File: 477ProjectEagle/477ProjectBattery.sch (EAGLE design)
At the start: 21 parts

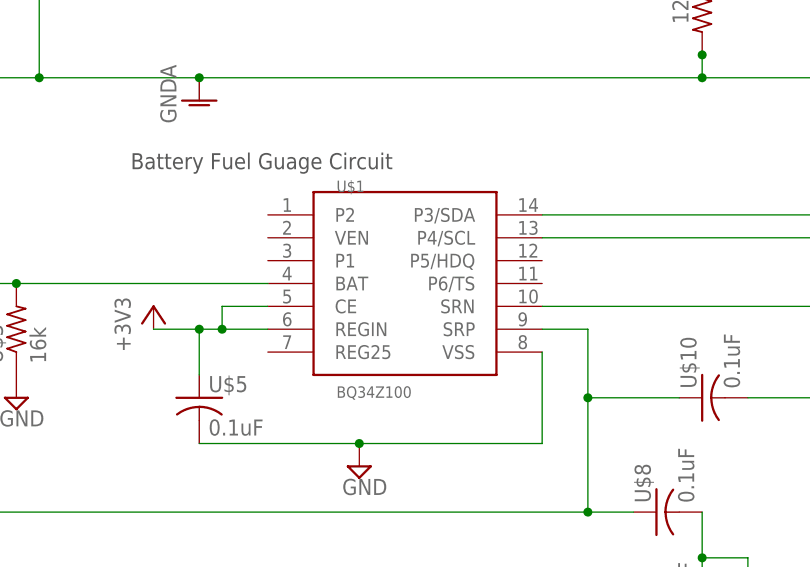
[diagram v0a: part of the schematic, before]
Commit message: Fixed Schematic to include cap for internal reg
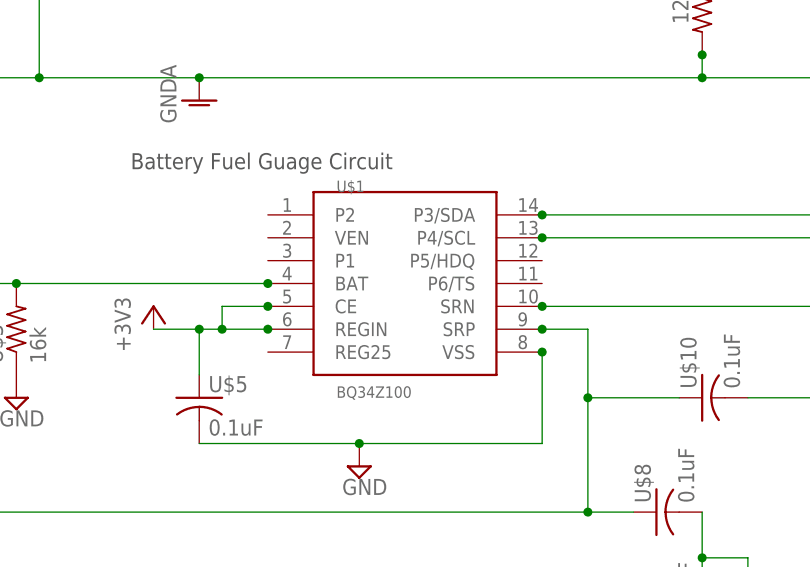
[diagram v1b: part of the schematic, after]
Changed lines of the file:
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@@
 <wire x1="-63.5" y1="-7.62" x2="-81.28" y2="-7.62" width="0.1524" layer="91"/>
 <junction x="-63.5" y="-7.62"/>
+<junction x="-43.18" y="2.54"/>
 </segment>
 <segment>
@@
 <junction x="-81.28" y="5.08"/>
 <junction x="-78.74" y="5.08"/>
+<junction x="-73.66" y="7.62"/>
+<junction x="-73.66" y="5.08"/>
 </segment>
 <segment>
@@
 <wire x1="-109.22" y1="10.16" x2="-101.6" y2="10.16" width="0.1524" layer="91"/>
 <junction x="-101.6" y="10.16"/>
+<junction x="-73.66" y="10.16"/>
 </segment>
 </net>
@@
 <wire x1="-43.18" y1="15.24" x2="38.1" y2="15.24" width="0.1524" layer="91"/>
 <pinref part="--" gate="-2" pin="S"/>
+<junction x="-43.18" y="15.24"/>
 </segment>
 </net>
@@
 <wire x1="-43.18" y1="17.78" x2="38.1" y2="17.78" width="0.1524" layer="91"/>
 <pinref part="--" gate="-1" pin="S"/>
+<junction x="-43.18" y="17.78"/>
 </segment>
 </net>
@@
 <pinref part="U$7" gate="G$1" pin="2"/>
 <wire x1="-132.08" y1="-17.78" x2="-119.38" y2="-17.78" width="0.1524" layer="91"/>
+<junction x="-43.18" y="7.62"/>
 </segment>
 </net>
@@
 <pinref part="U$6" gate="G$1" pin="2"/>
 <wire x1="-114.3" y1="-5.08" x2="-132.08" y2="-5.08" width="0.1524" layer="91"/>
+<junction x="-43.18" y="5.08"/>
 </segment>
 </net>

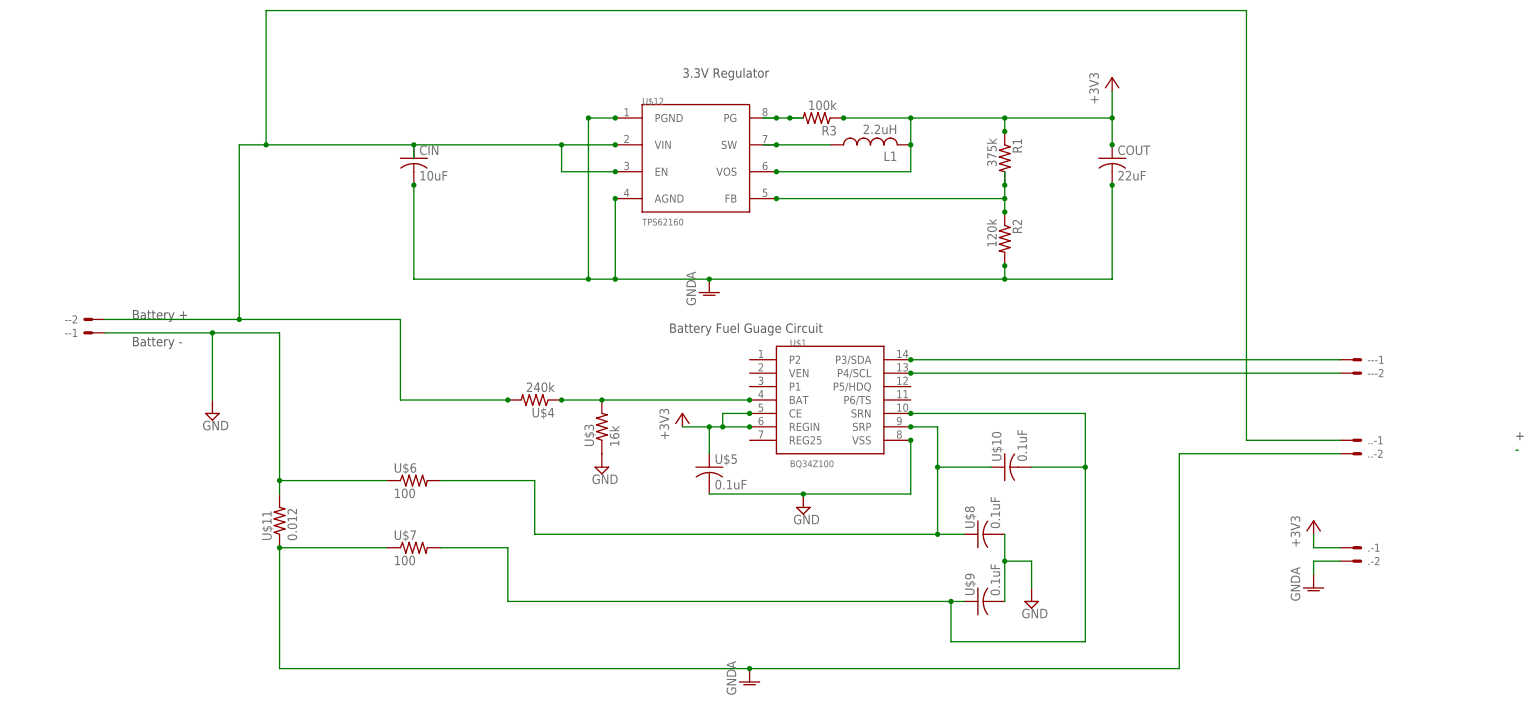
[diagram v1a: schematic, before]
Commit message: PCB is almost finalized.
Scott Lab- Added bulk cap. added GND plane. Added lots of information on
the silkscreen. Barrel connectors for all power sources. Verified and
fixed programming header(added cap). Added barrel connectors to battery
PCB and made standoff drill holes.
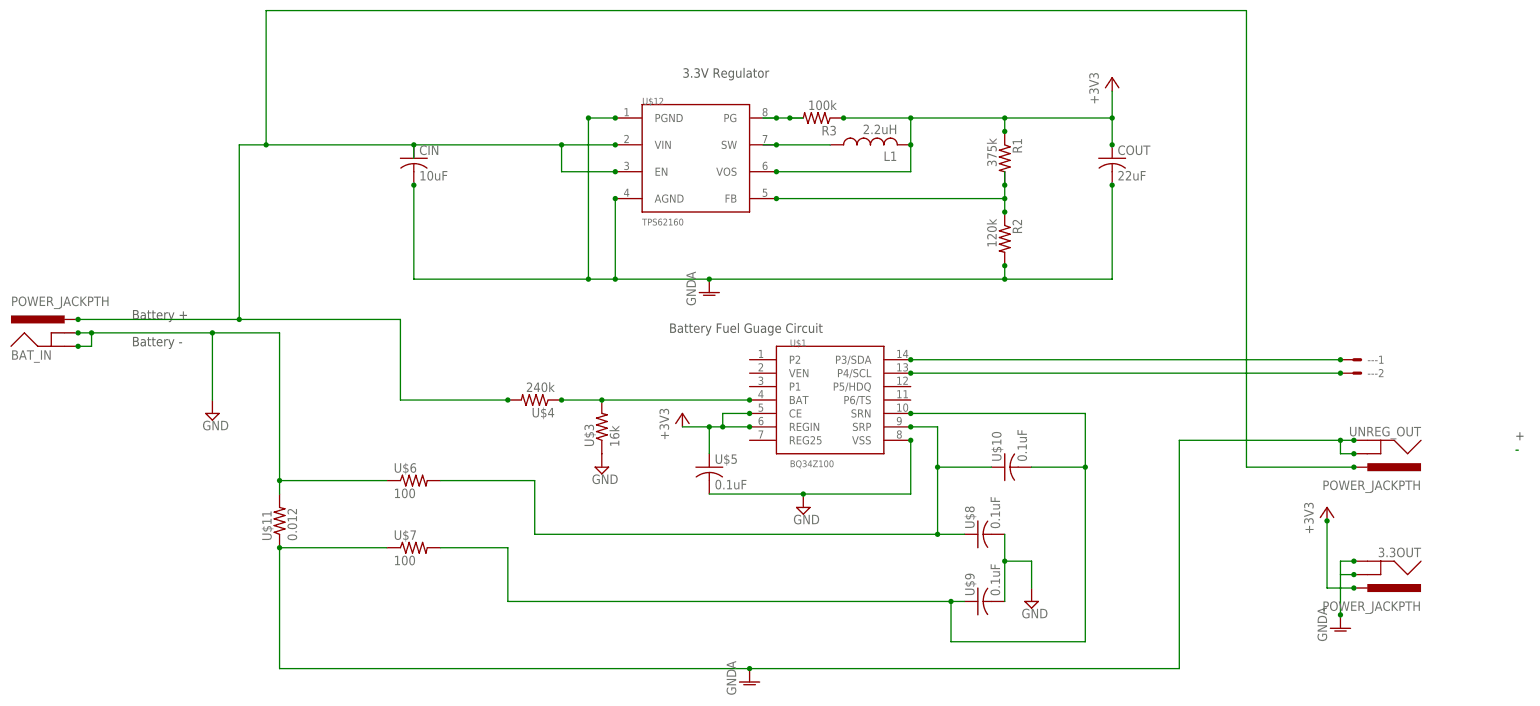
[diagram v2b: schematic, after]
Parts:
- removed -, ., ..: 22-23-2021, con-molex:22-23-2021
- added 3.3OUT, BAT_IN, UNREG_OUT: POWER_JACKPTH, SparkFun-Connectors:POWER_JACKPTH
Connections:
- net +3V3: now also 3.3OUT.PWR; no longer .-1.S
- net GND: now also BAT_IN.GND, BAT_IN.GNDBREAK; no longer --1.S
- net GNDA: now also 3.3OUT.GND, 3.3OUT.GNDBREAK, UNREG_OUT.GND, UNREG_OUT.GNDBREAK; no longer .-2.S, ..-2.S
- net N$4: now also BAT_IN.PWR, UNREG_OUT.PWR; no longer --2.S, ..-1.S
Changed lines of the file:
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@@
 <layers>
 <layer number="1" name="Top" color="4" fill="1" visible="no" active="no"/>
+<layer number="2" name="Route2" color="1" fill="3" visible="no" active="no"/>
+<layer number="3" name="Route3" color="4" fill="3" visible="no" active="no"/>
+<layer number="4" name="Route4" color="1" fill="4" visible="no" active="no"/>
+<layer number="5" name="Route5" color="4" fill="4" visible="no" active="no"/>
+<layer number="6" name="Route6" color="1" fill="8" visible="no" active="no"/>
+<layer number="7" name="Route7" color="4" fill="8" visible="no" active="no"/>
+<layer number="8" name="Route8" color="1" fill="2" visible="no" active="no"/>
+<layer number="9" name="Route9" color="4" fill="2" visible="no" active="no"/>
+<layer number="10" name="Route10" color="1" fill="7" visible="no" active="no"/>
+<layer number="11" name="Route11" color="4" fill="7" visible="no" active="no"/>
+<layer number="12" name="Route12" color="1" fill="5" visible="no" active="no"/>
+<layer number="13" name="Route13" color="4" fill="5" visible="no" active="no"/>
+<layer number="14" name="Route14" color="1" fill="6" visible="no" active="no"/>
+<layer number="15" name="Route15" color="4" fill="6" visible="no" active="no"/>
 <layer number="16" name="Bottom" color="1" fill="1" visible="no" active="no"/>
 <layer number="17" name="Pads" color="2" fill="1" visible="no" active="no"/>
@@
 <part name="SUPPLY2" library="supply2" deviceset="GND" device=""/>
 <part name="U$5" library="MinotaurParts" deviceset="C-US-1206" device="" value="0.1uF"/>
-<part name="-" library="con-molex" deviceset="22-23-2021" device="" value=""/>
 <part name="U$6" library="MinotaurParts" deviceset="R-US" device="&quot;" value="100"/>
 <part name="U$7" library="MinotaurParts" deviceset="R-US" device="&quot;" value="100"/>
@@
 <part name="SUPPLY3" library="supply2" deviceset="GND" device=""/>
 <part name="--" library="con-molex" deviceset="22-23-2021" device="" value=""/>
-<part name=".." library="con-molex" deviceset="22-23-2021" device="" value=""/>
 <part name="SUPPLY4" library="supply2" deviceset="GND" device=""/>
 <part name="GND1" library="supply1" deviceset="GNDA" device=""/>
 <part name="GND2" library="supply1" deviceset="GNDA" device=""/>
-<part name="." library="con-molex" deviceset="22-23-2021" device="" value=""/>
 <part name="GND3" library="supply1" deviceset="GNDA" device=""/>
 <part name="+3V3" library="supply1" deviceset="+3V3" device=""/>
 <part name="U$11" library="MinotaurParts" deviceset="R-US" device="CS" value="0.012"/>
+<part name="3.3OUT" library="SparkFun-Connectors" deviceset="POWER_JACK" device="PTH"/>
+<part name="UNREG_OUT" library="SparkFun-Connectors" deviceset="POWER_JACK" device="PTH"/>
+<part name="BAT_IN" library="SparkFun-Connectors" deviceset="POWER_JACK" device="PTH"/>
 </parts>
 <sheets>
@@
 <instance part="SUPPLY2" gate="GND" x="-63.5" y="-10.16"/>
 <instance part="U$5" gate="G$1" x="-81.28" y="-2.54"/>
-<instance part="-" gate="-1" x="-198.12" y="22.86" rot="R180"/>
-<instance part="-" gate="-2" x="-198.12" y="25.4" rot="R180"/>
 <instance part="U$6" gate="G$1" x="-137.16" y="-5.08"/>
 <instance part="U$7" gate="G$1" x="-137.16" y="-17.78"/>
@@
 <instance part="--" gate="-1" x="40.64" y="17.78"/>
 <instance part="--" gate="-2" x="40.64" y="15.24"/>
-<instance part=".." gate="-1" x="40.64" y="2.54"/>
-<instance part=".." gate="-2" x="40.64" y="0"/>
 <instance part="SUPPLY4" gate="GND" x="-175.26" y="7.62"/>
 <instance part="GND1" gate="1" x="-81.28" y="30.48"/>
 <instance part="GND2" gate="1" x="-73.66" y="-43.18"/>
-<instance part="." gate="-1" x="40.64" y="-17.78"/>
-<instance part="." gate="-2" x="40.64" y="-20.32"/>
-<instance part="GND3" gate="1" x="33.02" y="-25.4"/>
-<instance part="+3V3" gate="G$1" x="33.02" y="-12.7"/>
+<instance part="GND3" gate="1" x="38.1" y="-33.02"/>
+<instance part="+3V3" gate="G$1" x="35.56" y="-10.16"/>
 <instance part="U$11" gate="G$1" x="-162.56" y="-12.7" rot="R90"/>
+<instance part="3.3OUT" gate="G$1" x="43.18" y="-17.78" rot="R180"/>
+<instance part="UNREG_OUT" gate="G$1" x="43.18" y="5.08" rot="R180"/>
+<instance part="BAT_IN" gate="G$1" x="-203.2" y="17.78"/>
 </instances>
 <busses>
@@
 </segment>
 <segment>
-<pinref part="-" gate="-1" pin="S"/>
-<wire x1="-195.58" y1="22.86" x2="-175.26" y2="22.86" width="0.1524" layer="91"/>
+<wire x1="-200.66" y1="22.86" x2="-198.12" y2="22.86" width="0.1524" layer="91"/>
+<wire x1="-198.12" y1="22.86" x2="-175.26" y2="22.86" width="0.1524" layer="91"/>
 <wire x1="-175.26" y1="22.86" x2="-162.56" y2="22.86" width="0.1524" layer="91"/>
 <wire x1="-162.56" y1="22.86" x2="-162.56" y2="-5.08" width="0.1524" layer="91"/>
@@
 <wire x1="-162.56" y1="-5.08" x2="-162.56" y2="-7.62" width="0.1524" layer="91"/>
 <junction x="-162.56" y="-5.08"/>
+<pinref part="BAT_IN" gate="G$1" pin="GNDBREAK"/>
+<wire x1="-198.12" y1="22.86" x2="-198.12" y2="20.32" width="0.1524" layer="91"/>
+<pinref part="BAT_IN" gate="G$1" pin="GND"/>
+<wire x1="-198.12" y1="20.32" x2="-200.66" y2="20.32" width="0.1524" layer="91"/>
+<junction x="-200.66" y="22.86"/>
+<junction x="-200.66" y="20.32"/>
+<junction x="-198.12" y="22.86"/>
 </segment>
 </net>
@@
 </segment>
 <segment>
-<pinref part="." gate="-1" pin="S"/>
-<wire x1="38.1" y1="-17.78" x2="33.02" y2="-17.78" width="0.1524" layer="91"/>
-<wire x1="33.02" y1="-17.78" x2="33.02" y2="-15.24" width="0.1524" layer="91"/>
+<pinref part="3.3OUT" gate="G$1" pin="PWR"/>
 <pinref part="+3V3" gate="G$1" pin="+3V3"/>
+<wire x1="40.64" y1="-25.4" x2="35.56" y2="-25.4" width="0.1524" layer="91"/>
+<wire x1="35.56" y1="-25.4" x2="35.56" y2="-12.7" width="0.1524" layer="91"/>
+<junction x="40.64" y="-25.4"/>
+<junction x="35.56" y="-12.7"/>
 </segment>
 </net>
@@
 <pinref part="--" gate="-2" pin="S"/>
 <junction x="-43.18" y="15.24"/>
+<junction x="38.1" y="15.24"/>
 </segment>
 </net>
@@
 <pinref part="--" gate="-1" pin="S"/>
 <junction x="-43.18" y="17.78"/>
+<junction x="38.1" y="17.78"/>
 </segment>
 </net>
 <net name="N$4" class="0">
 <segment>
-<pinref part="-" gate="-2" pin="S"/>
-<wire x1="-170.18" y1="25.4" x2="-195.58" y2="25.4" width="0.1524" layer="91"/>
+<wire x1="-170.18" y1="25.4" x2="-200.66" y2="25.4" width="0.1524" layer="91"/>
 <wire x1="-170.18" y1="25.4" x2="-170.18" y2="58.42" width="0.1524" layer="91"/>
 <pinref part="CIN" gate="G$1" pin="1"/>
@@
 <wire x1="-165.1" y1="58.42" x2="-165.1" y2="83.82" width="0.1524" layer="91"/>
 <wire x1="-165.1" y1="83.82" x2="20.32" y2="83.82" width="0.1524" layer="91"/>
-<wire x1="20.32" y1="83.82" x2="20.32" y2="2.54" width="0.1524" layer="91"/>
-<wire x1="20.32" y1="2.54" x2="38.1" y2="2.54" width="0.1524" layer="91"/>
+<wire x1="20.32" y1="83.82" x2="20.32" y2="-2.54" width="0.1524" layer="91"/>
 <junction x="-165.1" y="58.42"/>
-<pinref part=".." gate="-1" pin="S"/>
+<pinref part="UNREG_OUT" gate="G$1" pin="PWR"/>
+<wire x1="20.32" y1="-2.54" x2="40.64" y2="-2.54" width="0.1524" layer="91"/>
+<junction x="40.64" y="-2.54"/>
+<pinref part="BAT_IN" gate="G$1" pin="PWR"/>
+<junction x="-200.66" y="25.4"/>
 </segment>
 </net>
@@
 <wire x1="-162.56" y1="-40.64" x2="-73.66" y2="-40.64" width="0.1524" layer="91"/>
 <wire x1="-73.66" y1="-40.64" x2="7.62" y2="-40.64" width="0.1524" layer="91"/>
-<wire x1="7.62" y1="-40.64" x2="7.62" y2="0" width="0.1524" layer="91"/>
-<wire x1="38.1" y1="0" x2="7.62" y2="0" width="0.1524" layer="91"/>
-<pinref part=".." gate="-2" pin="S"/>
+<wire x1="7.62" y1="-40.64" x2="7.62" y2="2.54" width="0.1524" layer="91"/>
 <pinref part="GND2" gate="1" pin="GNDA"/>
 <junction x="-73.66" y="-40.64"/>
 <pinref part="U$11" gate="G$1" pin="1"/>
 <junction x="-162.56" y="-17.78"/>
-</segment>
-<segment>
-<pinref part="." gate="-2" pin="S"/>
-<wire x1="38.1" y1="-20.32" x2="33.02" y2="-20.32" width="0.1524" layer="91"/>
-<wire x1="33.02" y1="-20.32" x2="33.02" y2="-22.86" width="0.1524" layer="91"/>
+<pinref part="UNREG_OUT" gate="G$1" pin="GND"/>
+<wire x1="7.62" y1="2.54" x2="38.1" y2="2.54" width="0.1524" layer="91"/>
+<wire x1="40.64" y1="2.54" x2="38.1" y2="2.54" width="0.1524" layer="91"/>
+<wire x1="38.1" y1="2.54" x2="38.1" y2="0" width="0.1524" layer="91"/>
+<pinref part="UNREG_OUT" gate="G$1" pin="GNDBREAK"/>
+<wire x1="38.1" y1="0" x2="40.64" y2="0" width="0.1524" layer="91"/>
+<junction x="40.64" y="2.54"/>
+<junction x="40.64" y="0"/>
+<junction x="38.1" y="2.54"/>
+</segment>
+<segment>
+<pinref part="3.3OUT" gate="G$1" pin="GND"/>
+<wire x1="40.64" y1="-20.32" x2="38.1" y2="-20.32" width="0.1524" layer="91"/>
+<wire x1="38.1" y1="-20.32" x2="38.1" y2="-22.86" width="0.1524" layer="91"/>
+<pinref part="3.3OUT" gate="G$1" pin="GNDBREAK"/>
+<wire x1="38.1" y1="-22.86" x2="38.1" y2="-30.48" width="0.1524" layer="91"/>
+<wire x1="40.64" y1="-22.86" x2="38.1" y2="-22.86" width="0.1524" layer="91"/>
 <pinref part="GND3" gate="1" pin="GNDA"/>
-</segment>
-</net>
+<junction x="40.64" y="-20.32"/>
+<junction x="40.64" y="-22.86"/>
+<junction x="38.1" y="-30.48"/>
+</segment>
+</net>

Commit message: Finishing touches on PCB
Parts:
- added U$2: 1uF, MinotaurParts:C-US-1206
- U$3: value 16k -> 16.5k
- U$4: value 240k -> 255k
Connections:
- new net N$7: U$1.REG25, U$2.1
- net GND: now also U$1.P1, U$1.P2, U$2.2
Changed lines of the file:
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@@
 <part name="L1" library="MinotaurParts" deviceset="SDR0403" device="" value="2.2uH"/>
 <part name="+3V2" library="supply1" deviceset="+3V3" device=""/>
-<part name="U$3" library="MinotaurParts" deviceset="R-US" device="&quot;" value="16k"/>
-<part name="U$4" library="MinotaurParts" deviceset="R-US" device="&quot;" value="240k"/>
+<part name="U$3" library="MinotaurParts" deviceset="R-US" device="&quot;" value="16.5k"/>
+<part name="U$4" library="MinotaurParts" deviceset="R-US" device="&quot;" value="255k"/>
 <part name="SUPPLY1" library="supply2" deviceset="GND" device=""/>
 <part name="SUPPLY2" library="supply2" deviceset="GND" device=""/>
@@
 <part name="UNREG_OUT" library="SparkFun-Connectors" deviceset="POWER_JACK" device="PTH"/>
 <part name="BAT_IN" library="SparkFun-Connectors" deviceset="POWER_JACK" device="PTH"/>
+<part name="U$2" library="MinotaurParts" deviceset="C-US-1206" device="" value="1uF"/>
+<part name="SUPPLY5" library="supply2" deviceset="GND" device=""/>
 </parts>
 <sheets>
@@
 <instance part="UNREG_OUT" gate="G$1" x="43.18" y="5.08" rot="R180"/>
 <instance part="BAT_IN" gate="G$1" x="-203.2" y="17.78"/>
+<instance part="U$2" gate="G$1" x="-73.66" y="-2.54"/>
+<instance part="SUPPLY5" gate="GND" x="-83.82" y="12.7"/>
 </instances>
 <busses>
@@
 <wire x1="-43.18" y1="-7.62" x2="-63.5" y2="-7.62" width="0.1524" layer="91"/>
 <pinref part="SUPPLY2" gate="GND" pin="GND"/>
-<wire x1="-63.5" y1="-7.62" x2="-81.28" y2="-7.62" width="0.1524" layer="91"/>
+<wire x1="-63.5" y1="-7.62" x2="-73.66" y2="-7.62" width="0.1524" layer="91"/>
 <junction x="-63.5" y="-7.62"/>
 <junction x="-43.18" y="2.54"/>
+<pinref part="U$2" gate="G$1" pin="2"/>
+<wire x1="-73.66" y1="-7.62" x2="-81.28" y2="-7.62" width="0.1524" layer="91"/>
+<junction x="-73.66" y="-7.62"/>
 </segment>
 <segment>
@@
 <pinref part="SUPPLY3" gate="GND" pin="GND"/>
 <junction x="-25.4" y="-20.32"/>
+<junction x="-25.4" y="-27.94"/>
+<junction x="-25.4" y="-15.24"/>
 </segment>
 <segment>
@@
 <junction x="-200.66" y="20.32"/>
 <junction x="-198.12" y="22.86"/>
+<junction x="-142.24" y="-5.08"/>
+</segment>
+<segment>
+<pinref part="U$1" gate="G$1" pin="P2"/>
+<wire x1="-73.66" y1="17.78" x2="-78.74" y2="17.78" width="0.1524" layer="91"/>
+<wire x1="-78.74" y1="17.78" x2="-83.82" y2="17.78" width="0.1524" layer="91"/>
+<wire x1="-83.82" y1="17.78" x2="-83.82" y2="15.24" width="0.1524" layer="91"/>
+<pinref part="U$1" gate="G$1" pin="P1"/>
+<wire x1="-73.66" y1="12.7" x2="-78.74" y2="12.7" width="0.1524" layer="91"/>
+<wire x1="-78.74" y1="12.7" x2="-78.74" y2="17.78" width="0.1524" layer="91"/>
+<pinref part="SUPPLY5" gate="GND" pin="GND"/>
+<junction x="-78.74" y="17.78"/>
+<junction x="-73.66" y="17.78"/>
+<junction x="-73.66" y="12.7"/>
+<junction x="-83.82" y="15.24"/>
 </segment>
 </net>
@@
 <pinref part="L1" gate="G$1" pin="2"/>
 <junction x="-43.18" y="58.42"/>
+<junction x="-5.08" y="68.58"/>
 </segment>
 <segment>
@@
 <wire x1="-132.08" y1="-17.78" x2="-119.38" y2="-17.78" width="0.1524" layer="91"/>
 <junction x="-43.18" y="7.62"/>
+<junction x="-132.08" y="-17.78"/>
+<junction x="-20.32" y="-2.54"/>
 </segment>
 </net>
@@
 <wire x1="-114.3" y1="-5.08" x2="-132.08" y2="-5.08" width="0.1524" layer="91"/>
 <junction x="-43.18" y="5.08"/>
+<junction x="-132.08" y="-5.08"/>
+<junction x="-33.02" y="-15.24"/>
+<junction x="-27.94" y="-2.54"/>
 </segment>
 </net>
@@
 <junction x="40.64" y="0"/>
 <junction x="38.1" y="2.54"/>
+<junction x="-142.24" y="-17.78"/>
 </segment>
 <segment>
@@
 </segment>
 </net>
+<net name="N$7" class="0">
+<segment>
+<pinref part="U$1" gate="G$1" pin="REG25"/>
+<pinref part="U$2" gate="G$1" pin="1"/>
+<wire x1="-73.66" y1="0" x2="-73.66" y2="2.54" width="0.1524" layer="91"/>
+<junction x="-73.66" y="2.54"/>
+<junction x="-73.66" y="0"/>
+</segment>
+</net>
